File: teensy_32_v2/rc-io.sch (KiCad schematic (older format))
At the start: 0 parts

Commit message: more hat
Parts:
- added U5, U6: CONN_03x08, teensy:CONN_03x08, symbol CONN_03x08
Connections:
- net labels added: +3.3VP, +5V, +BATT, CRX, CTX, GND, IN_AUX, IN_STEER, IN_THROTTLE, OUT_AUX, OUT_STEER, OUT_THROTTLE, T_A8, T_A9, T_CRX, T_CTX, T_RX1, T_RX2, T_TX1, T_TX2
- wire segments 0 -> 34

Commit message: another attempt at Hat layout -- pre routing
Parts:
- removed U5: CONN_03x08, teensy:CONN_03x08, symbol CONN_03x08
- added J7: M20-9980845, Pin_Headers:Pin_Header_Straight_2x08_Pitch2.54mm, symbol Conn_02x08_Odd_Even
- added J8: M20-9970445, Pin_Headers:Pin_Header_Straight_2x04_Pitch2.54mm, symbol Conn_02x04_Odd_Even
- J9: renamed from U6; value CONN_03x08 -> Drive
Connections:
- net labels added: T_RX3, T_SCL, T_SDA, T_TX3
- net labels removed: +3.3VP
- wire segments 34 -> 39

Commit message: Macrofab proto order of teensy hat v2b
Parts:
- J9: value Drive -> TSW-108-07-G-T
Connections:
- net labels added: +12V
- net labels removed: +BATT
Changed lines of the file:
@@
 $EndDescr
 $Comp
-L GND #PWR026
+L GND #PWR025
 U 1 1 59F81478
 P 9150 4300
-F 0 "#PWR026" H 9150 4050 50  0001 C CNN
+F 0 "#PWR025" H 9150 4050 50  0001 C CNN
 F 1 "GND" H 9150 4150 50  0000 C CNN
 F 2 "" H 9150 4300 50  0001 C CNN
@@
 $EndComp
 $Comp
-L +5V #PWR027
+L +5V #PWR026
 U 1 1 59F8151A
 P 7950 2450
-F 0 "#PWR027" H 7950 2300 50  0001 C CNN
+F 0 "#PWR026" H 7950 2300 50  0001 C CNN
 F 1 "+5V" H 7950 2590 50  0000 C CNN
 F 2 "" H 7950 2450 50  0001 C CNN
 F 3 "" H 7950 2450 50  0001 C CNN
 	1    7950 2450
-	1    0    0    -1
-$EndComp
-$Comp
-L +BATT #PWR028
-U 1 1 59F81530
-P 9300 2600
-F 0 "#PWR028" H 9300 2450 50  0001 C CNN
-F 1 "+BATT" H 9300 2740 50  0000 C CNN
-F 2 "" H 9300 2600 50  0001 C CNN
-F 3 "" H 9300 2600 50  0001 C CNN
-	1    9300 2600
 	1    0    0    -1
 $EndComp
@@
 IN_STEER
 $Comp
-L +5V #PWR029
+L +5V #PWR027
 U 1 1 59F820B2
 P 4550 2550
-F 0 "#PWR029" H 4550 2400 50  0001 C CNN
+F 0 "#PWR027" H 4550 2400 50  0001 C CNN
 F 1 "+5V" H 4550 2690 50  0000 C CNN
 F 2 "" H 4550 2550 50  0001 C CNN
@@
 T_TX2
 $Comp
-L GND #PWR030
+L GND #PWR028
 U 1 1 59F82B8B
 P 3800 4500
-F 0 "#PWR030" H 3800 4250 50  0001 C CNN
+F 0 "#PWR028" H 3800 4250 50  0001 C CNN
 F 1 "GND" H 3800 4350 50  0000 C CNN
 F 2 "" H 3800 4500 50  0001 C CNN
@@
 P 8500 3600
 F 0 "J9" H 8750 4300 60  0000 C CNN
-F 1 "Drive" H 8550 3200 60  0000 C CNN
+F 1 "TSW-108-07-G-T" H 8550 3200 60  0000 C CNN
 F 2 "teensy:CONN_03x08" H 8500 3600 60  0001 C CNN
 F 3 "" H 8500 3600 60  0000 C CNN
@@
 Connection ~ 8700 3400
 Connection ~ 8700 3500
+$Comp
+L +12V #PWR029
+U 1 1 5A1C2C5E
+P 9300 2600
+F 0 "#PWR029" H 9300 2450 50  0001 C CNN
+F 1 "+12V" H 9300 2740 50  0000 C CNN
+F 2 "" H 9300 2600 50  0001 C CNN
+F 3 "" H 9300 2600 50  0001 C CNN
+	1    9300 2600
+	1    0    0    -1
+$EndComp
 $EndSCHEMATC

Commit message: version 2017-12-30 of hat
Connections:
- net T_RX1: now also J7.3 (Pin_3); no longer J7.1 (Pin_1)
- net T_RX2: now also J7.12 (Pin_12); no longer J7.10 (Pin_10)
- net T_RX3: now also J8.4 (Pin_4); no longer J8.2 (Pin_2)
- net T_TX1: now also J7.1 (Pin_1); no longer J7.3 (Pin_3)
- net T_TX2: now also J7.10 (Pin_10); no longer J7.12 (Pin_12)
- net T_TX3: now also J8.2 (Pin_2); no longer J8.4 (Pin_4)
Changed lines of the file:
@@
 $EndDescr
 $Comp
-L GND #PWR028
+L GND #PWR030
 U 1 1 59F81478
 P 9150 4300
-F 0 "#PWR028" H 9150 4050 50  0001 C CNN
+F 0 "#PWR030" H 9150 4050 50  0001 C CNN
 F 1 "GND" H 9150 4150 50  0000 C CNN
 F 2 "" H 9150 4300 50  0001 C CNN
@@
 $EndComp
 $Comp
-L +5V #PWR029
+L +5V #PWR031
 U 1 1 59F8151A
 P 7950 2450
-F 0 "#PWR029" H 7950 2300 50  0001 C CNN
+F 0 "#PWR031" H 7950 2300 50  0001 C CNN
 F 1 "+5V" H 7950 2590 50  0000 C CNN
 F 2 "" H 7950 2450 50  0001 C CNN
@@
 IN_STEER
 $Comp
-L +5V #PWR030
+L +5V #PWR032
 U 1 1 59F820B2
 P 4550 2550
-F 0 "#PWR030" H 4550 2400 50  0001 C CNN
+F 0 "#PWR032" H 4550 2400 50  0001 C CNN
 F 1 "+5V" H 4550 2690 50  0000 C CNN
 F 2 "" H 4550 2550 50  0001 C CNN
@@
 	1    0    0    -1
 $EndComp
+Text Label 3300 2800 0    60   ~ 0
+T_RX1
 Text Label 3300 2700 0    60   ~ 0
-T_RX1
-Text Label 3300 2800 0    60   ~ 0
 T_TX1
 Text Label 3300 3100 0    60   ~ 0
@@
 Text Label 3300 3200 0    60   ~ 0
 CRX
+Text Label 5100 3200 2    60   ~ 0
+T_RX2
 Text Label 5100 3100 2    60   ~ 0
-T_RX2
-Text Label 5100 3200 2    60   ~ 0
 T_TX2
 $Comp
-L GND #PWR031
+L GND #PWR033
 U 1 1 59F82B8B
 P 3800 4500
-F 0 "#PWR031" H 3800 4250 50  0001 C CNN
+F 0 "#PWR033" H 3800 4250 50  0001 C CNN
 F 1 "GND" H 3800 4350 50  0000 C CNN
 F 2 "" H 3800 4500 50  0001 C CNN
@@
 Text Label 5100 2700 2    60   ~ 0
 T_A9
+Text HLabel 3250 2800 0    60   Input ~ 0
+T_RX1
 Text HLabel 3250 2700 0    60   Input ~ 0
-T_RX1
-Text HLabel 3250 2800 0    60   Input ~ 0
 T_TX1
 Text HLabel 3250 3100 0    60   Input ~ 0
@@
 Text HLabel 5150 2700 2    60   Input ~ 0
 T_A9
+Text HLabel 5150 3200 2    60   Input ~ 0
+T_RX2
 Text HLabel 5150 3100 2    60   Input ~ 0
-T_RX2
-Text HLabel 5150 3200 2    60   Input ~ 0
 T_TX2
 $Comp
@@
 Text HLabel 3250 4100 0    60   Input ~ 0
 T_SCL
+Text HLabel 5150 4100 2    60   Input ~ 0
+T_RX3
 Text HLabel 5150 4000 2    60   Input ~ 0
-T_RX3
-Text HLabel 5150 4100 2    60   Input ~ 0
 T_TX3
 Text Label 3300 4000 0    60   ~ 0
@@
 Text Label 3300 4100 0    60   ~ 0
 T_SCL
+Text Label 5100 4100 2    60   ~ 0
+T_RX3
 Text Label 5100 4000 2    60   ~ 0
-T_RX3
-Text Label 5100 4100 2    60   ~ 0
 T_TX3
 $Comp
@@
 Connection ~ 8700 3500
 $Comp
-L +12V #PWR032
+L +12V #PWR034
 U 1 1 5A1C2C5E
 P 9300 2600
-F 0 "#PWR032" H 9300 2450 50  0001 C CNN
+F 0 "#PWR034" H 9300 2450 50  0001 C CNN
 F 1 "+12V" H 9300 2740 50  0000 C CNN
 F 2 "" H 9300 2600 50  0001 C CNN

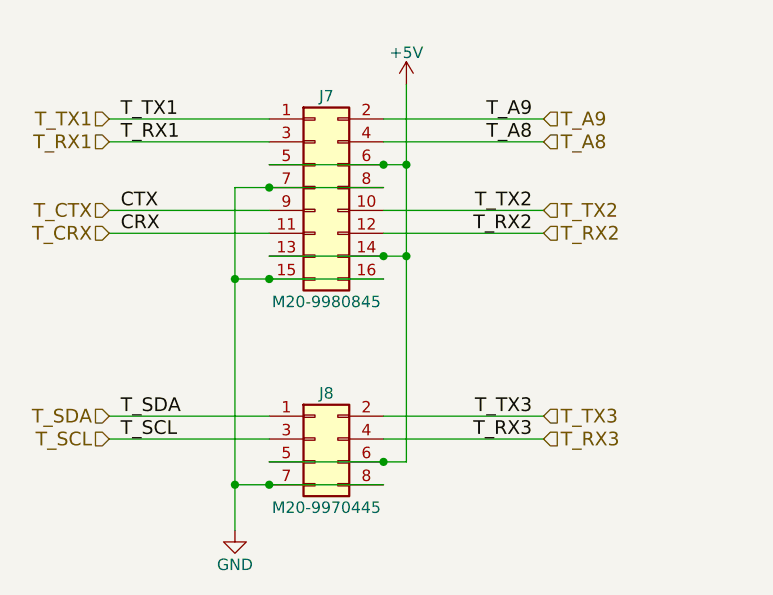
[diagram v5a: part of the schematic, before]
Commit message: make I2C/RPiUART port supply 3V.
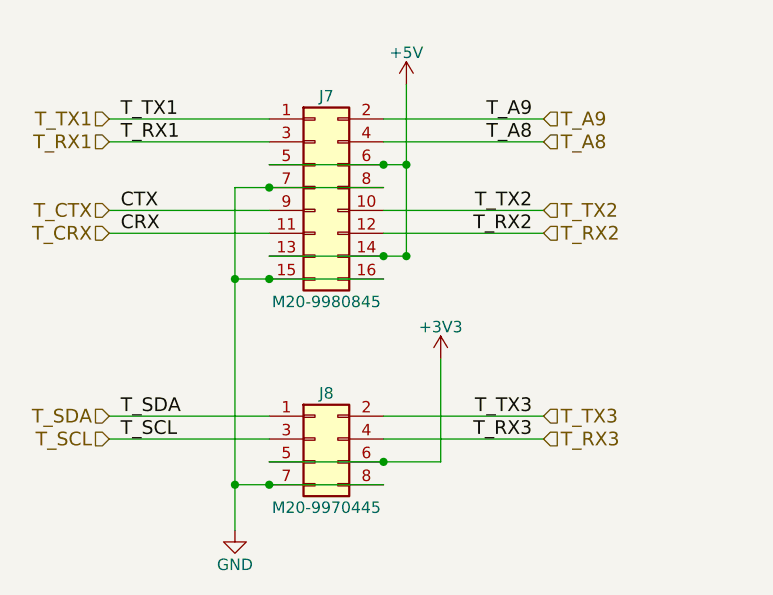
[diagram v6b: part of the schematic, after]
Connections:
- net +5V: no longer J8.5 (Pin_5), J8.6 (Pin_6)
- new net +3V3: J8.5 (Pin_5), J8.6 (Pin_6)
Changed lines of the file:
@@
 	4450 4100 5150 4100
 Wire Wire Line
-	4550 4200 4550 2550
+	4550 3300 4550 2550
 Wire Wire Line
 	3950 2900 4550 2900
@@
 	1    0    0    -1
 $EndComp
-Wire Wire Line
-	3950 4200 4550 4200
 Connection ~ 4550 3300
-Connection ~ 4450 4200
 Wire Wire Line
 	3800 4300 4450 4300
@@
 	1    0    0    -1
 $EndComp
+Wire Wire Line
+	3950 4200 4700 4200
+Wire Wire Line
+	4700 4200 4700 3750
+Connection ~ 4450 4200
+$Comp
+L +3V3 #PWR?
+U 1 1 5A495654
+P 4700 3750
+F 0 "#PWR?" H 4700 3600 50  0001 C CNN
+F 1 "+3V3" H 4700 3890 50  0000 C CNN
+F 2 "" H 4700 3750 50  0001 C CNN
+F 3 "" H 4700 3750 50  0001 C CNN
+	1    4700 3750
+	1    0    0    -1
+$EndComp
